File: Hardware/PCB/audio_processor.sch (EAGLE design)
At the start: 26 parts, among them J1 TMS-101-51-G-D, J10 TMS-101-51-G-D, J11 MTMM-101-X-X-S-X, J12 TMS-101-51-G-D, J2 MTMM-101-X-X-S-X, J3 TMS-101-51-G-D, J4 MTMM-101-X-X-S-X, J5 MTMM-101-X-X-S-X, J6 MTMM-101-X-X-S-X, J7 MTMM-101-X-X-S-X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

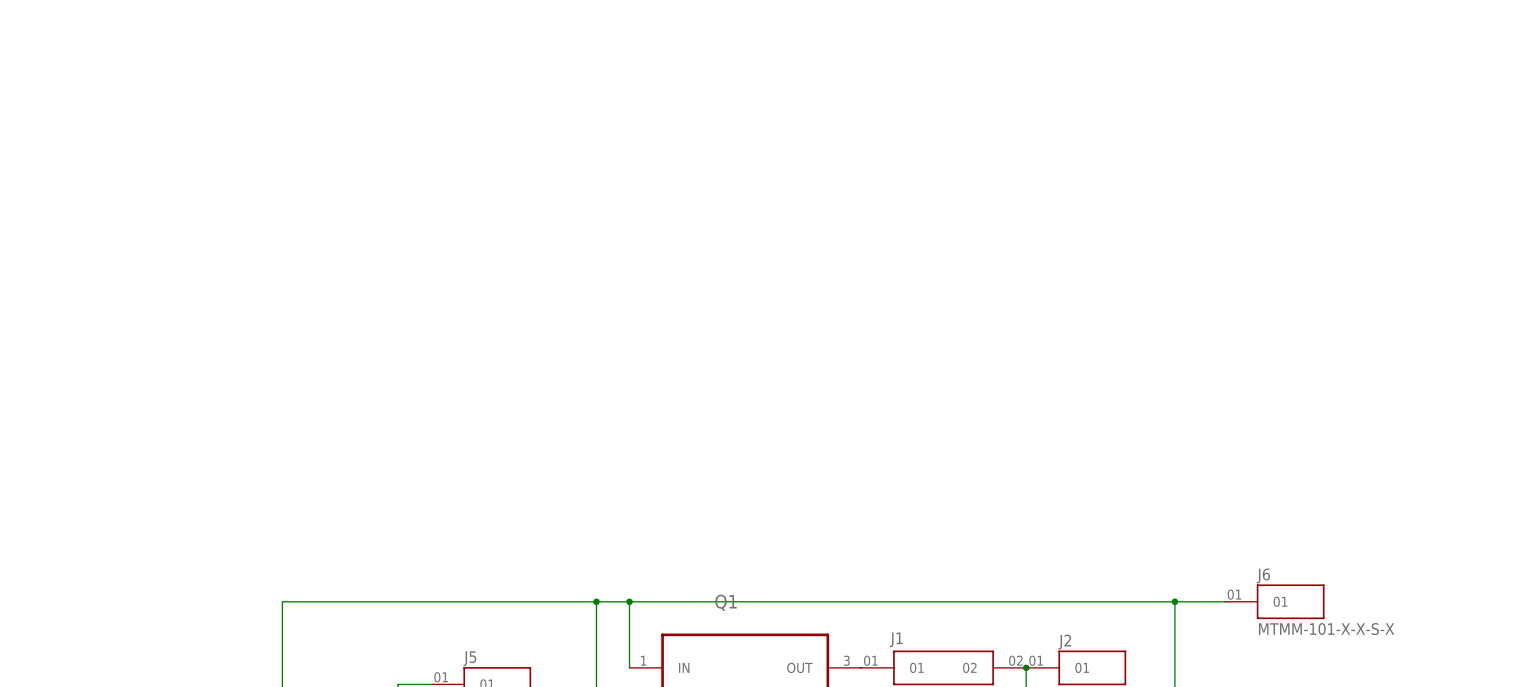
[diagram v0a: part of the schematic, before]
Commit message: AP_0_01
Added C code from Midifier product.
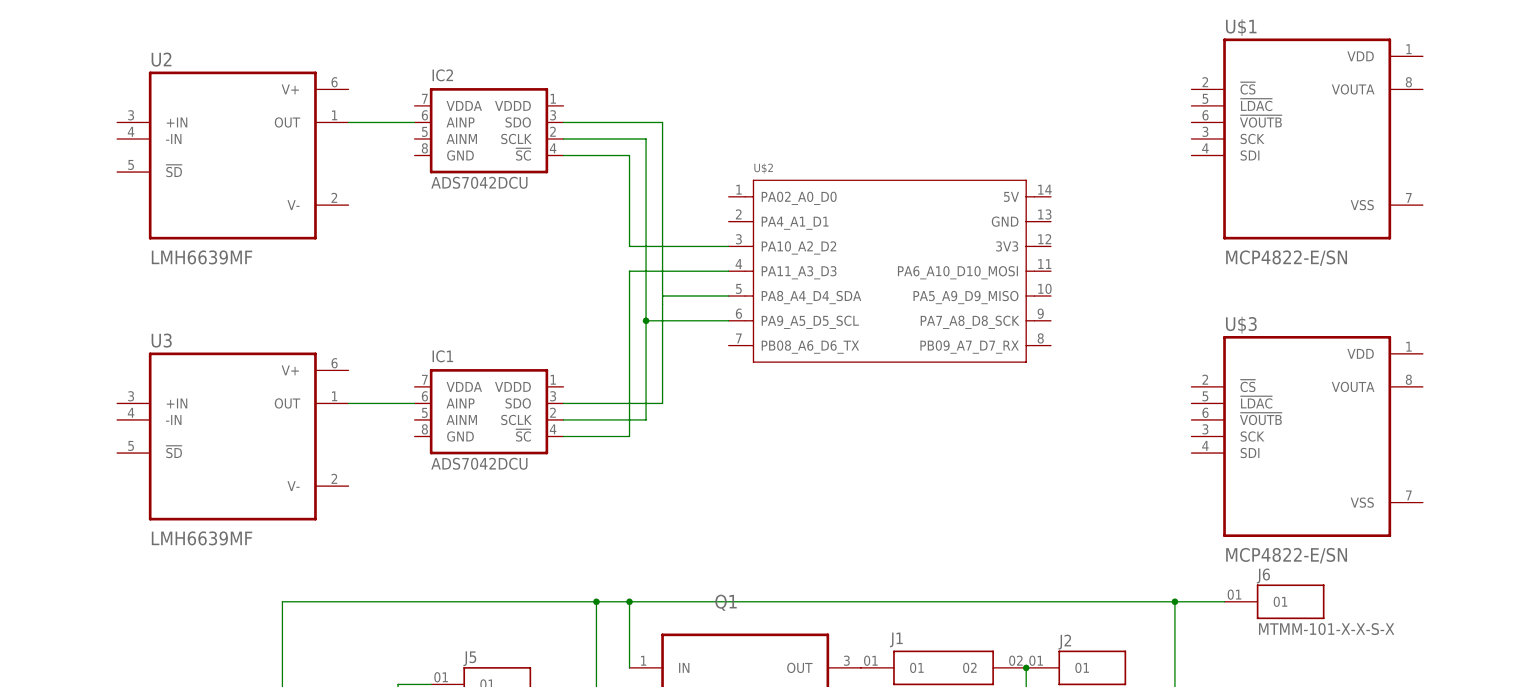
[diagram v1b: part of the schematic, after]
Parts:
- added IC1, IC2: ADS7042DCU, Texas Instruments:ADS7042DCU
- added U$1, U$3: MCP4822-E/SN, MCP4822-E_SN:MCP4822-E/SN
- added U$2: (no value), XIAO-ESP32C3:SEEED_ESP32_C3
- added U2, U3: LMH6639MF, LMH6639MF:LMH6639MF
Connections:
- new net N$21: IC1.SCLK, IC2.SCLK, U$2.PA9_A5_D5_SCL
- new net N$22: IC2.AINP, U2.OUT
- new net N$23: IC1.AINP, U3.OUT
- new net N$24: IC1.SDO, IC2.SDO, U$2.PA8_A4_D4_SDA
- new net N$25: IC1.!SC, U$2.PA11_A3_D3
- new net N$26: IC2.!SC, U$2.PA10_A2_D2
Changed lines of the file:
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@@
 <layer number="112" name="tSilk" color="7" fill="1" visible="no" active="yes"/>
 <layer number="113" name="ReferenceLS" color="7" fill="1" visible="no" active="no"/>
+<layer number="114" name="FRNTMAAT1" color="7" fill="1" visible="no" active="no"/>
+<layer number="115" name="FRNTMAAT2" color="7" fill="1" visible="no" active="no"/>
 <layer number="116" name="Patch_BOT" color="9" fill="4" visible="no" active="yes"/>
+<layer number="117" name="BACKMAAT1" color="7" fill="1" visible="no" active="no"/>
 <layer number="118" name="Rect_Pads" color="7" fill="1" visible="no" active="no"/>
+<layer number="119" name="KAP_TEKEN" color="7" fill="1" visible="no" active="no"/>
+<layer number="120" name="KAP_MAAT1" color="7" fill="1" visible="no" active="no"/>
 <layer number="121" name="_tsilk" color="7" fill="1" visible="no" active="yes"/>
 <layer number="122" name="_bsilk" color="7" fill="1" visible="no" active="yes"/>
@@
 <layer number="128" name="_bValues" color="7" fill="1" visible="no" active="yes"/>
 <layer number="129" name="Mask" color="7" fill="1" visible="yes" active="yes"/>
+<layer number="130" name="SMDSTROOK" color="7" fill="1" visible="no" active="no"/>
 <layer number="131" name="tAdjust" color="7" fill="1" visible="no" active="yes"/>
 <layer number="132" name="bAdjust" color="7" fill="1" visible="no" active="yes"/>
+<layer number="133" name="bottom_silk" color="7" fill="1" visible="no" active="no"/>
+<layer number="134" name="silk_top" color="5" fill="1" visible="no" active="no"/>
+<layer number="135" name="silk_bottom" color="7" fill="1" visible="no" active="no"/>
+<layer number="136" name="silktop" color="7" fill="1" visible="no" active="no"/>
+<layer number="137" name="silkbottom" color="7" fill="1" visible="no" active="no"/>
+<layer number="138" name="NEw" color="7" fill="1" visible="no" active="no"/>
+<layer number="139" name="mtKeepout" color="7" fill="1" visible="no" active="no"/>
+<layer number="140" name="mbKeepout" color="7" fill="1" visible="no" active="no"/>
+<layer number="141" name="mtRestrict" color="7" fill="1" visible="no" active="no"/>
+<layer number="142" name="mbRestrict" color="7" fill="1" visible="no" active="no"/>
+<layer number="143" name="mvRestrict" color="7" fill="1" visible="no" active="no"/>
 <layer number="144" name="Drill_legend" color="7" fill="1" visible="no" active="yes"/>
+<layer number="145" name="DrillLegend_01-16" color="7" fill="1" visible="no" active="no"/>
+<layer number="146" name="DrillLegend_01-20" color="7" fill="1" visible="no" active="no"/>
+<layer number="147" name="mMeasures" color="7" fill="1" visible="no" active="no"/>
+<layer number="148" name="mDocument" color="7" fill="1" visible="no" active="no"/>
+<layer number="149" name="mReference" color="7" fill="1" visible="no" active="no"/>
 <layer number="150" name="Notes" color="7" fill="1" visible="no" active="yes"/>
 <layer number="151" name="HeatSink" color="7" fill="1" visible="no" active="yes"/>
@@
 <layer number="154" name="FabDoc2" color="2" fill="1" visible="no" active="no"/>
 <layer number="155" name="FabDoc3" color="7" fill="15" visible="no" active="no"/>
+<layer number="156" name="DXF0409-TOP" color="7" fill="1" visible="no" active="no"/>
+<layer number="157" name="DXF0409-BOTTOM" color="7" fill="1" visible="no" active="no"/>
+<layer number="166" name="AntennaArea" color="7" fill="1" visible="no" active="no"/>
+<layer number="168" name="4mmHeightArea" color="7" fill="1" visible="no" active="no"/>
+<layer number="191" name="mNets" color="7" fill="1" visible="no" active="no"/>
+<layer number="192" name="mBusses" color="7" fill="1" visible="no" active="no"/>
+<layer number="193" name="mPins" color="7" fill="1" visible="no" active="no"/>
+<layer number="194" name="mSymbols" color="7" fill="1" visible="no" active="no"/>
+<layer number="195" name="mNames" color="7" fill="1" visible="no" active="no"/>
+<layer number="196" name="mValues" color="7" fill="1" visible="no" active="no"/>
 <layer number="199" name="Contour" color="7" fill="1" visible="no" active="yes"/>
 <layer number="200" name="200bmp" color="1" fill="10" visible="no" active="yes"/>
@@
 <part name="J8" library="MTMM-101-X-X-S-X" deviceset="MTMM-101-X-X-S-X" device=""/>
 <part name="B1" library="Net_bridge" deviceset="NET_BRIDGE" device="" package3d_urn="urn:adsk.eagle:package:39213142/1"/>
+<part name="IC1" library="Texas Instruments" deviceset="ADS7042" device="DCU" package3d_urn="urn:adsk.eagle:package:7566972/2"/>
+<part name="U$1" library="MCP4822-E_SN" deviceset="MCP4822-E/SN" device=""/>
+<part name="U$2" library="XIAO-ESP32C3" deviceset="SEEED_ESP32_C3" device=""/>
+<part name="U2" library="LMH6639MF" deviceset="LMH6639MF" device="">
+<attribute name="LCSC" value="C131982"/>
+</part>
+<part name="U3" library="LMH6639MF" deviceset="LMH6639MF" device="">
+<attribute name="LCSC" value="C131982"/>
+</part>
+<part name="IC2" library="Texas Instruments" deviceset="ADS7042" device="DCU" package3d_urn="urn:adsk.eagle:package:7566972/2"/>
+<part name="U$3" library="MCP4822-E_SN" deviceset="MCP4822-E/SN" device=""/>
 </parts>
 <sheets>
@@
 </instance>
 <instance part="B1" gate="G$1" x="233.8" y="31.57" smashed="yes"/>
+<instance part="IC1" gate="G$1" x="127" y="144.78" smashed="yes">
+<attribute name="NAME" x="119.38" y="151.13" size="1.778" layer="95"/>
+<attribute name="VALUE" x="119.38" y="134.62" size="1.778" layer="96"/>
+</instance>
+<instance part="U$1" gate="A" x="254" y="185.42" smashed="yes">
+<attribute name="NAME" x="241.3" y="201.66" size="2.0828" layer="95" ratio="10" rot="SR0"/>
+<attribute name="VALUE" x="241.3" y="166.18" size="2.0828" layer="96" ratio="10" rot="SR0"/>
+</instance>
+<instance part="U$2" gate="G$1" x="190.5" y="165.1" smashed="yes">
+<attribute name="NAME" x="168.91" y="180.34" size="1.27" layer="95" ratio="12"/>
+<attribute name="VALUE" x="168.91" y="179.07" size="1.27" layer="96" ratio="12"/>
+</instance>
+<instance part="U2" gate="A" x="88.9" y="182.88" smashed="yes">
+<attribute name="NAME" x="76.2" y="196.58" size="2.0828" layer="95" ratio="10" rot="SR0"/>
+<attribute name="VALUE" x="76.2" y="166.18" size="2.0828" layer="96" ratio="10" rot="SR0"/>
+<attribute name="LCSC" x="88.9" y="182.88" size="1.778" layer="96" display="off"/>
+</instance>
+<instance part="U3" gate="A" x="88.9" y="139.7" smashed="yes">
+<attribute name="NAME" x="76.2" y="153.4" size="2.0828" layer="95" ratio="10" rot="SR0"/>
+<attribute name="VALUE" x="76.2" y="123" size="2.0828" layer="96" ratio="10" rot="SR0"/>
+<attribute name="LCSC" x="88.9" y="139.7" size="1.778" layer="96" display="off"/>
+</instance>
+<instance part="IC2" gate="G$1" x="127" y="187.96" smashed="yes">
+<attribute name="NAME" x="119.38" y="194.31" size="1.778" layer="95"/>
+<attribute name="VALUE" x="119.38" y="177.8" size="1.778" layer="96"/>
+</instance>
+<instance part="U$3" gate="A" x="254" y="139.7" smashed="yes">
+<attribute name="NAME" x="241.3" y="155.94" size="2.0828" layer="95" ratio="10" rot="SR0"/>
+<attribute name="VALUE" x="241.3" y="120.46" size="2.0828" layer="96" ratio="10" rot="SR0"/>
+</instance>
 </instances>
 <busses>
@@
 </segment>
 </net>
+<net name="N$21" class="0">
+<segment>
+<pinref part="IC1" gate="G$1" pin="SCLK"/>
+<pinref part="IC2" gate="G$1" pin="SCLK"/>
+<wire x1="139.7" y1="185.42" x2="152.4" y2="185.42" width="0.1524" layer="91"/>
+<wire x1="152.4" y1="185.42" x2="152.4" y2="157.48" width="0.1524" layer="91"/>
+<wire x1="152.4" y1="157.48" x2="152.4" y2="142.24" width="0.1524" layer="91"/>
+<wire x1="152.4" y1="142.24" x2="139.7" y2="142.24" width="0.1524" layer="91"/>
+<pinref part="U$2" gate="G$1" pin="PA9_A5_D5_SCL"/>
+<wire x1="165.1" y1="157.48" x2="152.4" y2="157.48" width="0.1524" layer="91"/>
+<junction x="152.4" y="157.48"/>
+</segment>
+</net>
+<net name="N$22" class="0">
+<segment>
+<pinref part="U2" gate="A" pin="OUT"/>
+<pinref part="IC2" gate="G$1" pin="AINP"/>
+<wire x1="106.68" y1="187.96" x2="116.84" y2="187.96" width="0.1524" layer="91"/>
+</segment>
+</net>
+<net name="N$23" class="0">
+<segment>
+<pinref part="U3" gate="A" pin="OUT"/>
+<pinref part="IC1" gate="G$1" pin="AINP"/>
+<wire x1="106.68" y1="144.78" x2="116.84" y2="144.78" width="0.1524" layer="91"/>
+</segment>
+</net>
+<net name="N$24" class="0">
+<segment>
+<pinref part="IC2" gate="G$1" pin="SDO"/>
+<wire x1="139.7" y1="187.96" x2="154.94" y2="187.96" width="0.1524" layer="91"/>
+<wire x1="154.94" y1="187.96" x2="154.94" y2="161.29" width="0.1524" layer="91"/>
+<pinref part="IC1" gate="G$1" pin="SDO"/>
+<wire x1="154.94" y1="160.02" x2="154.94" y2="144.78" width="0.1524" layer="91"/>
+<wire x1="154.94" y1="144.78" x2="139.7" y2="144.78" width="0.1524" layer="91"/>
+<pinref part="U$2" gate="G$1" pin="PA8_A4_D4_SDA"/>
+<wire x1="165.1" y1="161.29" x2="154.94" y2="161.29" width="0.1524" layer="91"/>
+<wire x1="154.94" y1="161.29" x2="154.94" y2="160.02" width="0.1524" layer="91"/>
+</segment>
+</net>
+<net name="N$25" class="0">
+<segment>
+<pinref part="IC1" gate="G$1" pin="!SC"/>
+<wire x1="139.7" y1="139.7" x2="149.86" y2="139.7" width="0.1524" layer="91"/>
+<pinref part="U$2" gate="G$1" pin="PA11_A3_D3"/>
+<wire x1="149.86" y1="139.7" x2="149.86" y2="165.1" width="0.1524" layer="91"/>
+<wire x1="149.86" y1="165.1" x2="165.1" y2="165.1" width="0.1524" layer="91"/>
+</segment>
+</net>
+<net name="N$26" class="0">
+<segment>
+<pinref part="IC2" gate="G$1" pin="!SC"/>
+<wire x1="139.7" y1="182.88" x2="149.86" y2="182.88" width="0.1524" layer="91"/>
+<pinref part="U$2" gate="G$1" pin="PA10_A2_D2"/>
+<wire x1="149.86" y1="182.88" x2="149.86" y2="168.91" width="0.1524" layer="91"/>
+<wire x1="149.86" y1="168.91" x2="165.1" y2="168.91" width="0.1524" layer="91"/>
+</segment>
+</net>
